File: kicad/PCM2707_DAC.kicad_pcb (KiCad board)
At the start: 2 copper layers, 49.5 x 38.1 mm, 37 parts, among them CON1 GND_CONNECTORSMD, J1 USB, Q1 12MHz, U1 PCM2707C

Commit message: Modified kicad files and corrected errors
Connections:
- J1 pad 2: /D+ -> /D-
- J1 pad 4: (no net) -> Net-(J1-Pad4)
- R7 pad 2: /D+ -> /D-
- SV1 pad 2: /D+ -> /D-
- U1 pad 14: (no net) -> Net-(U1-Pad14)
- U1 pad 18: (no net) -> Net-(U1-Pad18)
- U1 pad 19: (no net) -> Net-(U1-Pad19)
- U1 pad 4: (no net) -> Net-(U1-Pad4)
- U1 pad 5: (no net) -> Net-(U1-Pad5)
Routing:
- net /D-: track 0.00 -> 18.9 mm, vias 0 -> 1
- net /D+: track 41.5 -> 22.6 mm, vias 2 -> 1
- net GND: track 33.5 -> 25.7 mm
- net AGND: track 27.5 -> 26.7 mm

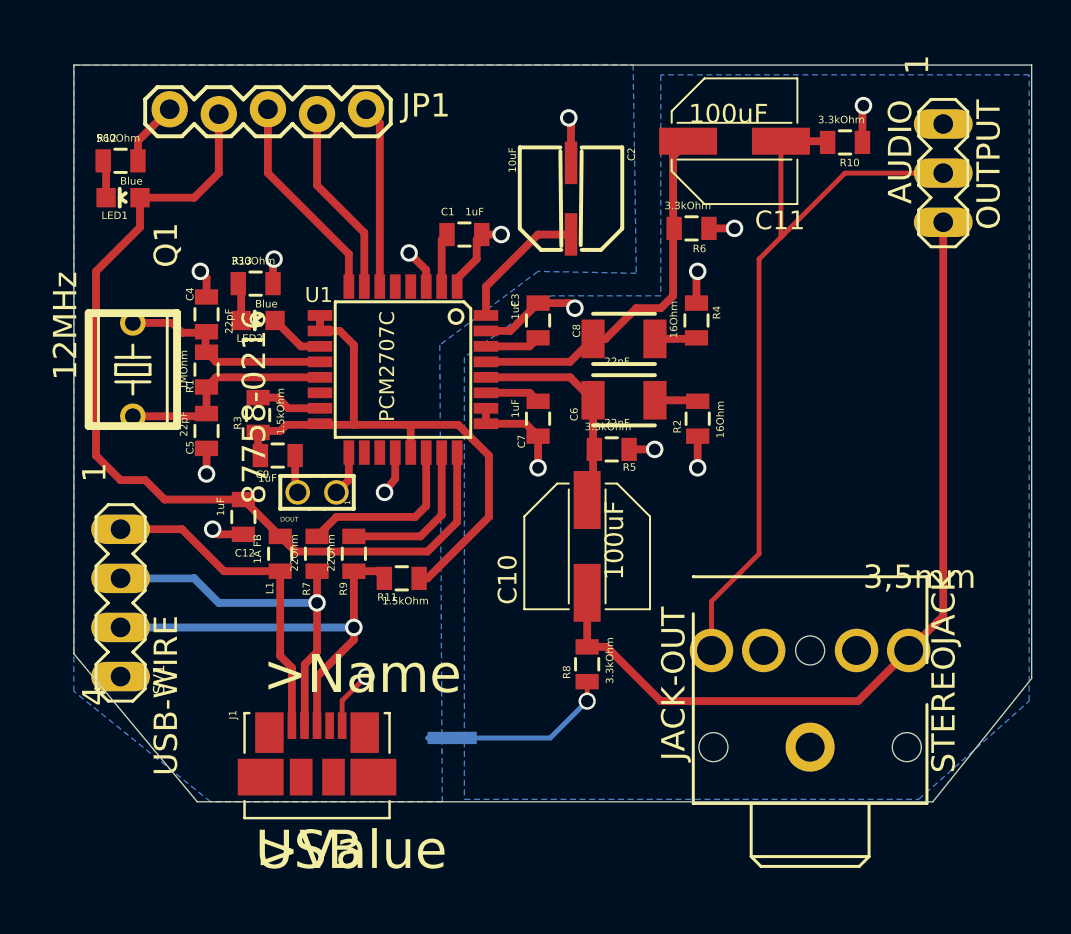
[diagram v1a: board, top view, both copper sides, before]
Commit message: Updated Schematic to use exported Eagle lbw
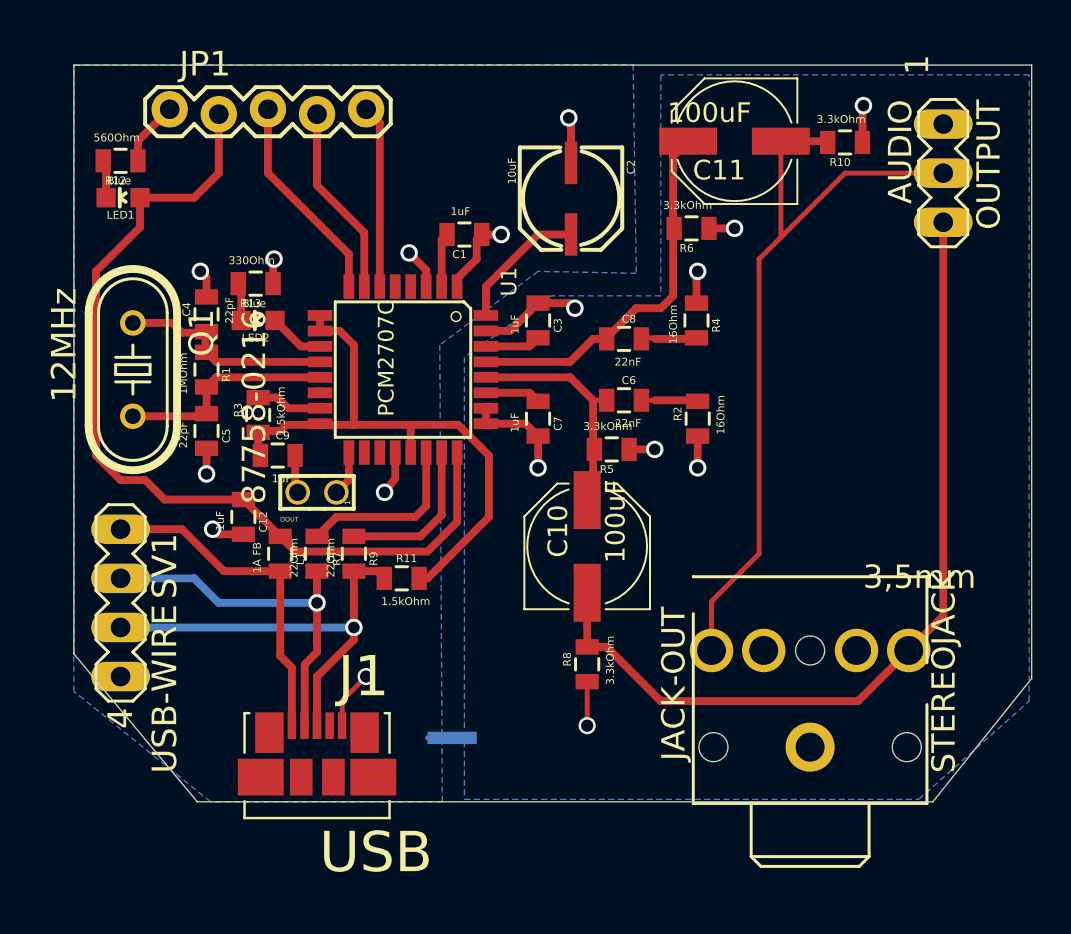
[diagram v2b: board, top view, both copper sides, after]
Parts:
- C1, C12, C3, C4, C5, C7, C9, L1, R1, R10, R11, R12, R13, R2, R3, R4, R5, R6, R7, R8, R9: footprint 0805 -> PCM2707_DAC:SPARKFUN-PASSIVES_0805
- C10, C11: footprint PANASONIC_D -> PCM2707_DAC:SPARKFUN-PASSIVES_PANASONIC_D
- C2: footprint PANASONIC_C -> PCM2707_DAC:SPARKFUN-PASSIVES_PANASONIC_C
- C6, C8: footprint 1210 -> PCM2707_DAC:SPARKFUN-PASSIVES_0805
- CON1: footprint GND_CONNECTOR -> PCM2707_DAC:LOWDERLIB_GND_CONNECTOR
- J1: footprint MOLEX_47346-0001 -> PCM2707_DAC:MOLEX-47346-0001_MOLEX_47346-0001
- JP1: footprint 1X05_LOCK -> PCM2707_DAC:SPARKFUN-CONNECTORS_1X05_LOCK
- LED1, LED2: footprint LED-0603 -> PCM2707_DAC:SPARKFUN-LED_LED-0603
- Q1: footprint HC49U-V -> PCM2707_DAC:CRYSTAL_HC49U-V
- SV1: footprint MA04-1 -> PCM2707_DAC:CON-LSTB_MA04-1
- U1: footprint 32TQFP_PCM2707C -> PCM2707_DAC:LOWDERLIB_32TQFP_PCM2707C
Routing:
- net AGND: track 26.7 -> 20.9 mm
- net /N$18: track 2.23 -> 5.16 mm
- net /N$17: track 2.17 -> 5.04 mm
- net /N$23: track 11.7 -> 12.4 mm

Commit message: Tidied up names, corrected PCB footprint
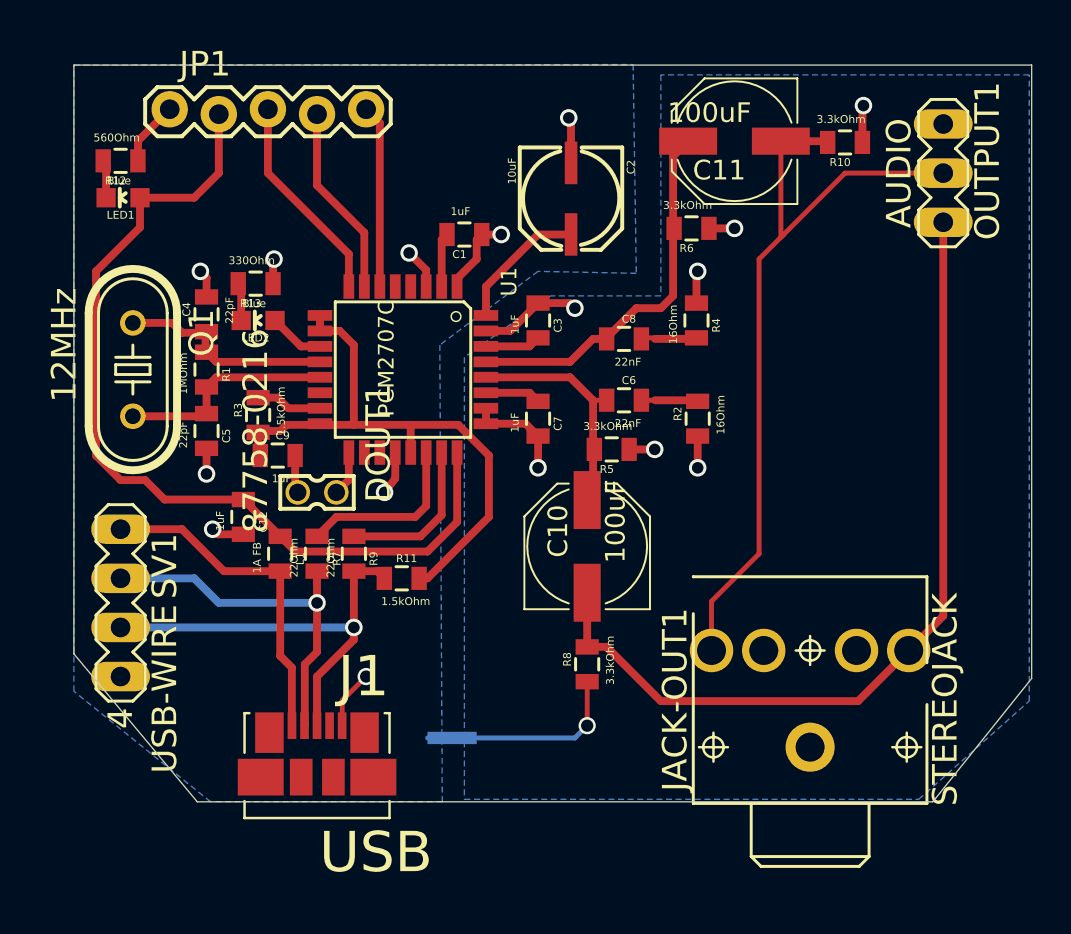
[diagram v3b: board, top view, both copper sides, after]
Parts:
- removed DOUT: 87758-0216, 87758-0216
- removed JACK-OUT: STEREOJACK, STX3100
- removed OUTPUT: AUDIO, MA03-1
- added DOUT1: 87758-0216, PCM2707_DAC:CON-MOLEX_87758-0216, F.Cu at (161.3, 78.1)
- added JACK-OUT1: STEREOJACK, PCM2707_DAC:STX3100, F.Cu at (186.7, 94.0)
- added OUTPUT1: AUDIO, PCM2707_DAC:CON-LSTB_MA03-1, F.Cu at (193.7, 61.6)
- CON1: footprint PCM2707_DAC:LOWDERLIB_GND_CONNECTOR -> PCM2707_DAC:GND_CONNECTOR
- U1: footprint PCM2707_DAC:LOWDERLIB_32TQFP_PCM2707C -> PCM2707_DAC:PCM2707C
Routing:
- net AGND: track 20.9 -> 27.5 mm
- net N$6: track 0.91 -> 0.00 mm
- net /N$6: track 1.41 -> 2.32 mm

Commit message: Removed library prefix from library files
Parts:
- C1, C12, C3, C4, C5, C6, C7, C8, C9, L1, R1, R10, R11, R12, R13, R2, R3, R4, R5, R6, R7, R8, R9: footprint PCM2707_DAC:SPARKFUN-PASSIVES_0805 -> PCM2707_DAC:PASSIVES_0805
- C10, C11: footprint PCM2707_DAC:SPARKFUN-PASSIVES_PANASONIC_D -> PCM2707_DAC:PASSIVES_PANASONIC_D
- C2: footprint PCM2707_DAC:SPARKFUN-PASSIVES_PANASONIC_C -> PCM2707_DAC:PASSIVES_PANASONIC_C
- JP1: footprint PCM2707_DAC:SPARKFUN-CONNECTORS_1X05_LOCK -> PCM2707_DAC:CONNECTORS_1X05_LOCK
- LED1, LED2: footprint PCM2707_DAC:SPARKFUN-LED_LED-0603 -> PCM2707_DAC:LED_LED-0603
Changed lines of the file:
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@@
     (links 79)
     (no_connects 0)
-    (area 147.0025 54.7497 198.259701 98.75012)
+    (area 148.704299 55.994299 198.259701 94.119701)
     (thickness 1.6)
     (drawings 6)
@@
       (net 25 GND))
   )
-  (module PCM2707_DAC:SPARKFUN-PASSIVES_0805 (layer Top)
+  (module PCM2707_DAC:PASSIVES_0805 (layer Top)
     (at 168.91 64.77 180)
     (attr smd)
@@
       (net 11 /N$2))
   )
-  (module PCM2707_DAC:SPARKFUN-PASSIVES_PANASONIC_C (layer Top)
+  (module PCM2707_DAC:PASSIVES_PANASONIC_C (layer Top)
     (at 174.625 62.865 270)
     (descr "PANASONIC ALUMINIUM ELECTROLYTIC CAPACITOR VS-SERIE PACKAGE E")
@@
       (net 25 GND))
   )
-  (module PCM2707_DAC:SPARKFUN-PASSIVES_0805 (layer Top)
+  (module PCM2707_DAC:PASSIVES_0805 (layer Top)
     (at 172.72 69.215 270)
     (attr smd)
@@
       (net 5 /N$13))
   )
-  (module PCM2707_DAC:SPARKFUN-PASSIVES_0805 (layer Top)
+  (module PCM2707_DAC:PASSIVES_0805 (layer Top)
     (at 155.575 68.8975 90)
     (attr smd)
@@
       (net 25 GND))
   )
-  (module PCM2707_DAC:SPARKFUN-PASSIVES_0805 (layer Top)
+  (module PCM2707_DAC:PASSIVES_0805 (layer Top)
     (at 155.575 74.93 270)
     (attr smd)
@@
       (net 25 GND))
   )
-  (module PCM2707_DAC:SPARKFUN-PASSIVES_0805 (layer Top)
+  (module PCM2707_DAC:PASSIVES_0805 (layer Top)
     (at 177.165 73.3425)
     (attr smd)
@@
       (net 10 /N$18))
   )
-  (module PCM2707_DAC:SPARKFUN-PASSIVES_0805 (layer Top)
+  (module PCM2707_DAC:PASSIVES_0805 (layer Top)
     (at 172.72 74.295 270)
     (attr smd)
@@
       (net 24 AGND))
   )
-  (module PCM2707_DAC:SPARKFUN-PASSIVES_0805 (layer Top)
+  (module PCM2707_DAC:PASSIVES_0805 (layer Top)
     (at 177.165 70.1675)
     (attr smd)
@@
       (net 9 /N$17))
   )
-  (module PCM2707_DAC:SPARKFUN-PASSIVES_0805 (layer Top)
+  (module PCM2707_DAC:PASSIVES_0805 (layer Top)
     (at 159.258 76.2)
     (attr smd)
@@
       (net 25 GND))
   )
-  (module PCM2707_DAC:SPARKFUN-PASSIVES_PANASONIC_D (layer Top)
+  (module PCM2707_DAC:PASSIVES_PANASONIC_D (layer Top)
     (at 175.26 80.899 90)
     (attr smd)
@@
       (net 26 OL))
   )
-  (module PCM2707_DAC:SPARKFUN-PASSIVES_PANASONIC_D (layer Top)
+  (module PCM2707_DAC:PASSIVES_PANASONIC_D (layer Top)
     (at 182.88 59.944 180)
     (attr smd)
@@
       (net 27 OR))
   )
-  (module PCM2707_DAC:SPARKFUN-PASSIVES_0805 (layer Top)
+  (module PCM2707_DAC:PASSIVES_0805 (layer Top)
     (at 157.48 79.375 270)
     (attr smd)
@@
     (pad M6 smd rect (at 2.91084 2.65938) (size 2.3749 1.89992) (layers Top F.Paste F.Mask))
   )
-  (module PCM2707_DAC:SPARKFUN-CONNECTORS_1X05_LOCK (layer Top)
+  (module PCM2707_DAC:CONNECTORS_1X05_LOCK (layer Top)
     (at 153.67 58.42)
     (attr virtual)
@@
       (net 3 /N$1))
   )
-  (module PCM2707_DAC:SPARKFUN-PASSIVES_0805 (layer Top)
+  (module PCM2707_DAC:PASSIVES_0805 (layer Top)
     (at 159.385 81.28 270)
     (attr smd)
@@
       (net 22 /VBUS))
   )
-  (module PCM2707_DAC:SPARKFUN-LED_LED-0603 (layer Top)
+  (module PCM2707_DAC:LED_LED-0603 (layer Top)
     (at 151.257 62.865 90)
     (attr smd)
@@
       (net 6 /N$14))
   )
-  (module PCM2707_DAC:SPARKFUN-LED_LED-0603 (layer Top)
+  (module PCM2707_DAC:LED_LED-0603 (layer Top)
     (at 158.242 69.215 90)
     (attr smd)
@@
       (net 20 /N$8))
   )
-  (module PCM2707_DAC:SPARKFUN-PASSIVES_0805 (layer Top)
+  (module PCM2707_DAC:PASSIVES_0805 (layer Top)
     (at 155.575 71.755 270)
     (attr smd)
@@
       (net 20 /N$8))
   )
-  (module PCM2707_DAC:SPARKFUN-PASSIVES_0805 (layer Top)
+  (module PCM2707_DAC:PASSIVES_0805 (layer Top)
     (at 180.975 74.295 90)
     (attr smd)
@@
       (net 10 /N$18))
   )
-  (module PCM2707_DAC:SPARKFUN-PASSIVES_0805 (layer Top)
+  (module PCM2707_DAC:PASSIVES_0805 (layer Top)
     (at 158.242 74.1045 90)
     (attr smd)
@@
       (net 7 /N$15))
   )
-  (module PCM2707_DAC:SPARKFUN-PASSIVES_0805 (layer Top)
+  (module PCM2707_DAC:PASSIVES_0805 (layer Top)
     (at 180.9115 69.215 270)
     (attr smd)
@@
       (net 9 /N$17))
   )
-  (module PCM2707_DAC:SPARKFUN-PASSIVES_0805 (layer Top)
+  (module PCM2707_DAC:PASSIVES_0805 (layer Top)
     (at 176.53 75.8825 180)
     (attr smd)
@@
       (net 14 /N$23))
   )
-  (module PCM2707_DAC:SPARKFUN-PASSIVES_0805 (layer Top)
+  (module PCM2707_DAC:PASSIVES_0805 (layer Top)
     (at 180.6575 64.4525 180)
     (attr smd)
@@
       (net 12 /N$21))
   )
-  (module PCM2707_DAC:SPARKFUN-PASSIVES_0805 (layer Top)
+  (module PCM2707_DAC:PASSIVES_0805 (layer Top)
     (at 161.29 81.28 270)
     (attr smd)
@@
       (net 29 /D-))
   )
-  (module PCM2707_DAC:SPARKFUN-PASSIVES_0805 (layer Top)
+  (module PCM2707_DAC:PASSIVES_0805 (layer Top)
     (at 175.26 86.995 90)
     (attr smd)
@@
       (net 26 OL))
   )
-  (module PCM2707_DAC:SPARKFUN-PASSIVES_0805 (layer Top)
+  (module PCM2707_DAC:PASSIVES_0805 (layer Top)
     (at 163.195 81.28 270)
     (attr smd)
@@
       (net 2 /D+))
   )
-  (module PCM2707_DAC:SPARKFUN-PASSIVES_0805 (layer Top)
+  (module PCM2707_DAC:PASSIVES_0805 (layer Top)
     (at 188.595 60.0075 180)
     (attr smd)
@@
       (net 27 OR))
   )
-  (module PCM2707_DAC:SPARKFUN-PASSIVES_0805 (layer Top)
+  (module PCM2707_DAC:PASSIVES_0805 (layer Top)
     (at 165.6715 82.55)
     (attr smd)
@@
       (net 28 VDD))
   )
-  (module PCM2707_DAC:SPARKFUN-PASSIVES_0805 (layer Top)
+  (module PCM2707_DAC:PASSIVES_0805 (layer Top)
     (at 151.13 60.96 180)
     (attr smd)
@@
       (net 6 /N$14))
   )
-  (module PCM2707_DAC:SPARKFUN-PASSIVES_0805 (layer Top)
+  (module PCM2707_DAC:PASSIVES_0805 (layer Top)
     (at 158.115 67.31 180)
     (attr smd)
